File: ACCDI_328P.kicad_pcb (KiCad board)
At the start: 2 copper layers, 150.1 x 82.2 mm, 44 parts, among them IC1 MJE340G, J1 Conn_01x05_Female, Q1 2N2222, Q2 2N2222, U1 LR8N3-G, U2 ATmega328P-P, Y1 16Mhz

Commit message: 2 layer board
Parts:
- added H7: Kill Switch, MountingHole:MountingHole_2.2mm_M2_Pad_TopBottom, F.Cu at (138.3, 115.9)
- R3: footprint Resistor_THT:R_Axial_DIN0516_L15.5mm_D5.0mm_P30.48mm_Horizontal -> Resistor_THT:R_Axial_DIN0516_L15.5mm_D5.0mm_P20.32mm_Horizontal
- Y1: value 16Mhz -> HC49S-16-30-50-70-30-ATF; footprint ABLS2-12:XTAL_ABLS2-12.000MHZ-B1U-T -> Crystal:Resonator-2Pin_W10.0mm_H5.0mm
- moved D2 93.9 mm to (114.9, 57.1)
- moved H4 87.5 mm to (163.4, 115.8)
- moved H3 76.3 mm to (170.9, 115.7)
- moved D3 58.7 mm to (173.4, 108.5)
- moved D5 58.2 mm to (90.8, 115.2), turned to 0 degrees
- moved R9 56.8 mm to (120.5, 115.1)
- moved C7 51.5 mm to (132.8, 69.2)
- moved D1 44.5 mm to (130.6, 62.9), turned to 0 degrees
- moved H5 43.3 mm to (132.1, 116.0)
- moved R6 42.5 mm to (159.8, 109.5)
- moved D8 41.0 mm to (134.4, 102.4)
- moved R4 38.2 mm to (152.7, 56.0), turned to 0 degrees
- moved R5 30.7 mm to (170.9, 56.0)
- moved C4 30.0 mm to (142.2, 71.3), turned to 0 degrees
- moved D7 27.6 mm to (154.9, 70.6)
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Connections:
- IC1 pad 3: Souce_coil -> Net-(IC1-Pad3)
- R4 pad 1: Souce_coil -> Net-(IC1-Pad3)
- U1 pad 2: Souce_coil -> Net-(IC1-Pad3)
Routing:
- net GND: track 425.9 -> 292.3 mm, vias 2 -> 0
- net Souce_coil: track 235.8 -> 132.4 mm
- net SCR_gate: track 128.8 -> 68.7 mm
- net +5 Volt: track 215.8 -> 176.5 mm, vias 5 -> 3
- net Net-(C12-Pad1): track 23.1 -> 59.9 mm
- net Net-(J1-Pad3): track 36.9 -> 73.7 mm
- net Pickup_circuit: track 40.9 -> 66.3 mm, vias 2 -> 0
- net Net-(D8-Pad1): track 18.8 -> 40.8 mm
- net Net-(C10-Pad1): track 48.4 -> 68.0 mm
- net Net-(C9-Pad1): track 20.0 -> 38.3 mm
- net Net-(IC1-Pad3): track 0.00 -> 15.7 mm
- net Net-(C8-Pad2): track 21.9 -> 32.0 mm
- net Net-(R4-Pad2): track 25.3 -> 16.5 mm
- net Net-(C5-Pad1): track 61.1 -> 55.5 mm
- net Net-(C1-Pad2): track 9.32 -> 5.17 mm
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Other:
- board size 150.1 x 82.2 mm -> 100 x 69.1 mm

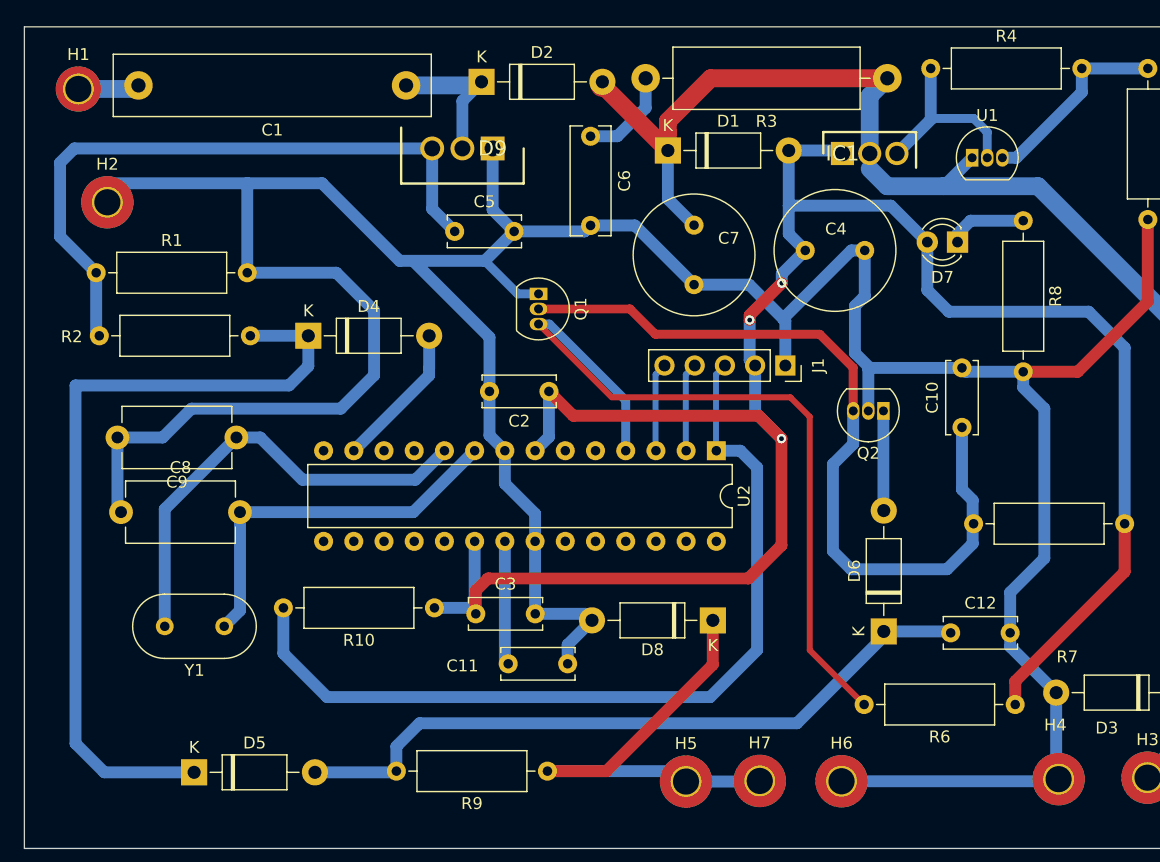
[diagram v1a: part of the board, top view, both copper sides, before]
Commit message: Modified track widths
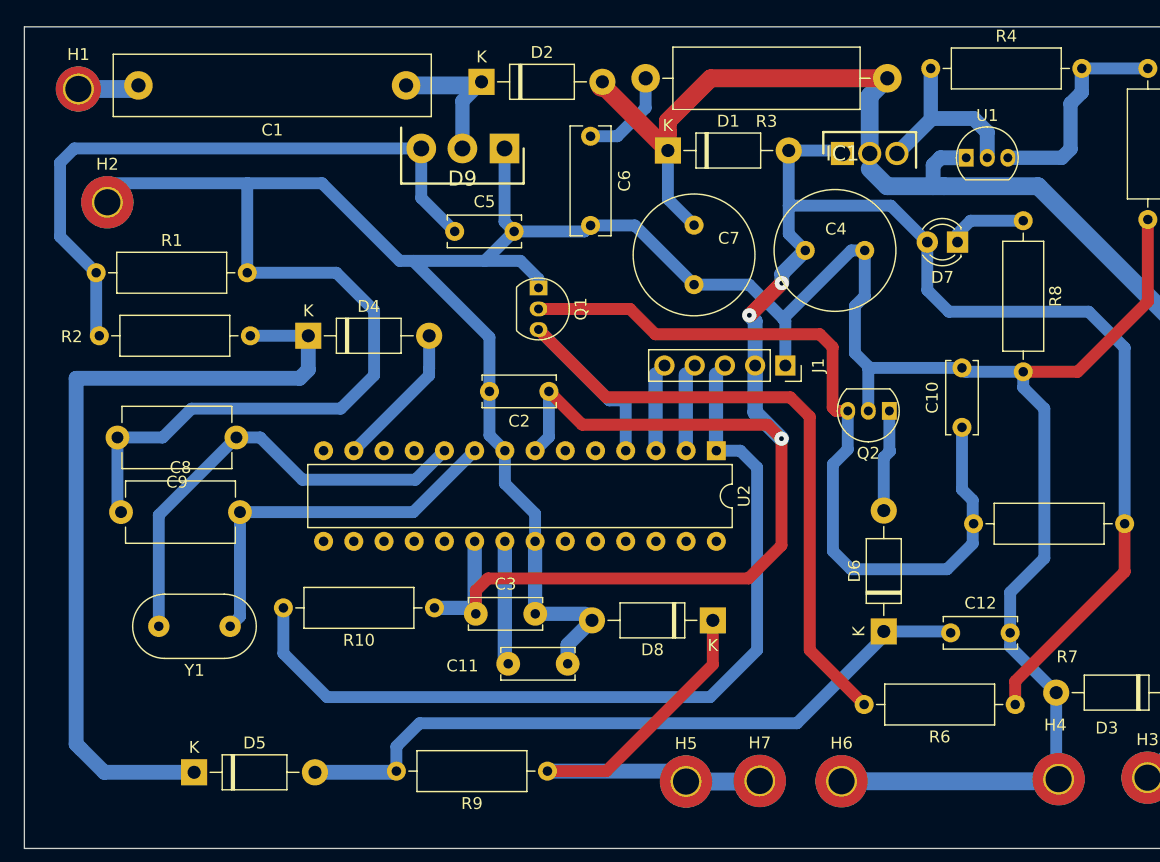
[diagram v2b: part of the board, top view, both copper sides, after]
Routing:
- net Net-(R4-Pad2): track 16.5 -> 18.3 mm
- net Souce_coil: track 132.4 -> 133.8 mm
- net SCR_gate: track 68.7 -> 69.8 mm
- net Net-(C5-Pad1): track 55.5 -> 54.9 mm

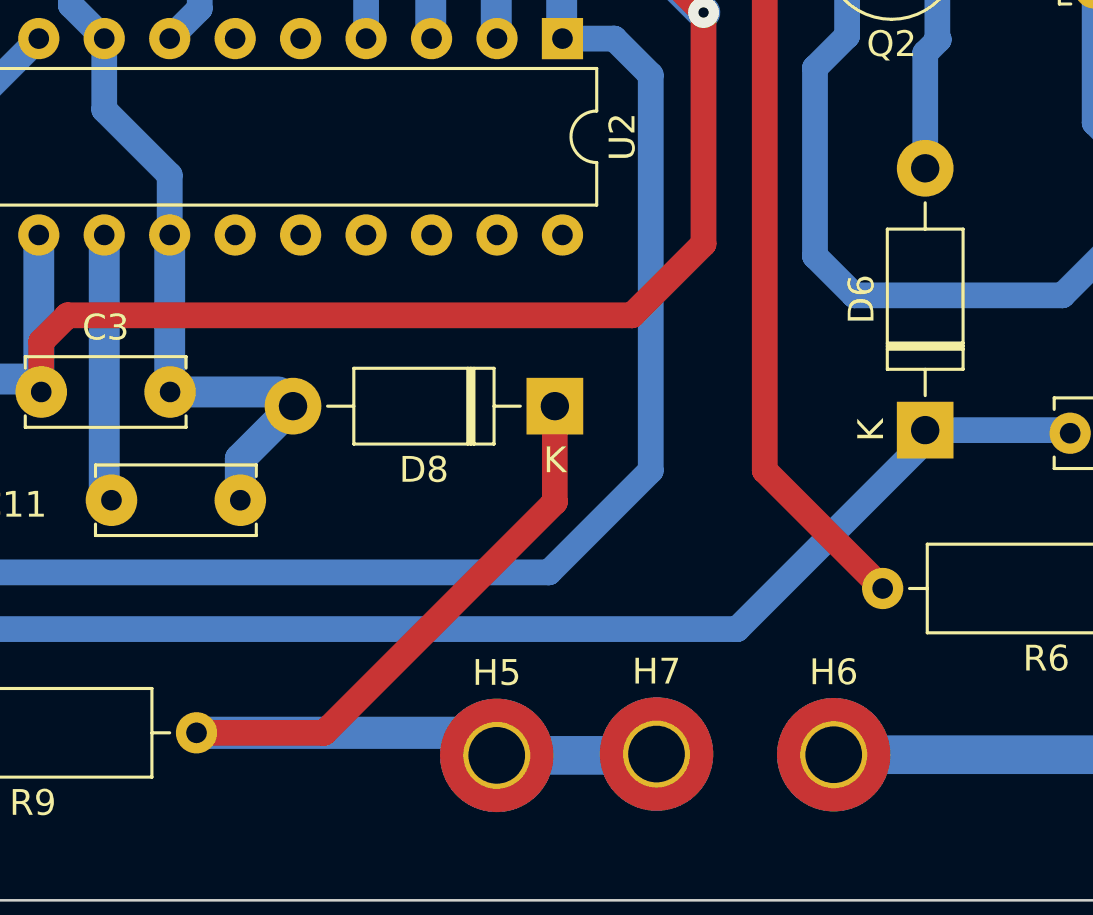
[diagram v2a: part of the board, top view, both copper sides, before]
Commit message: Removed zenner diode
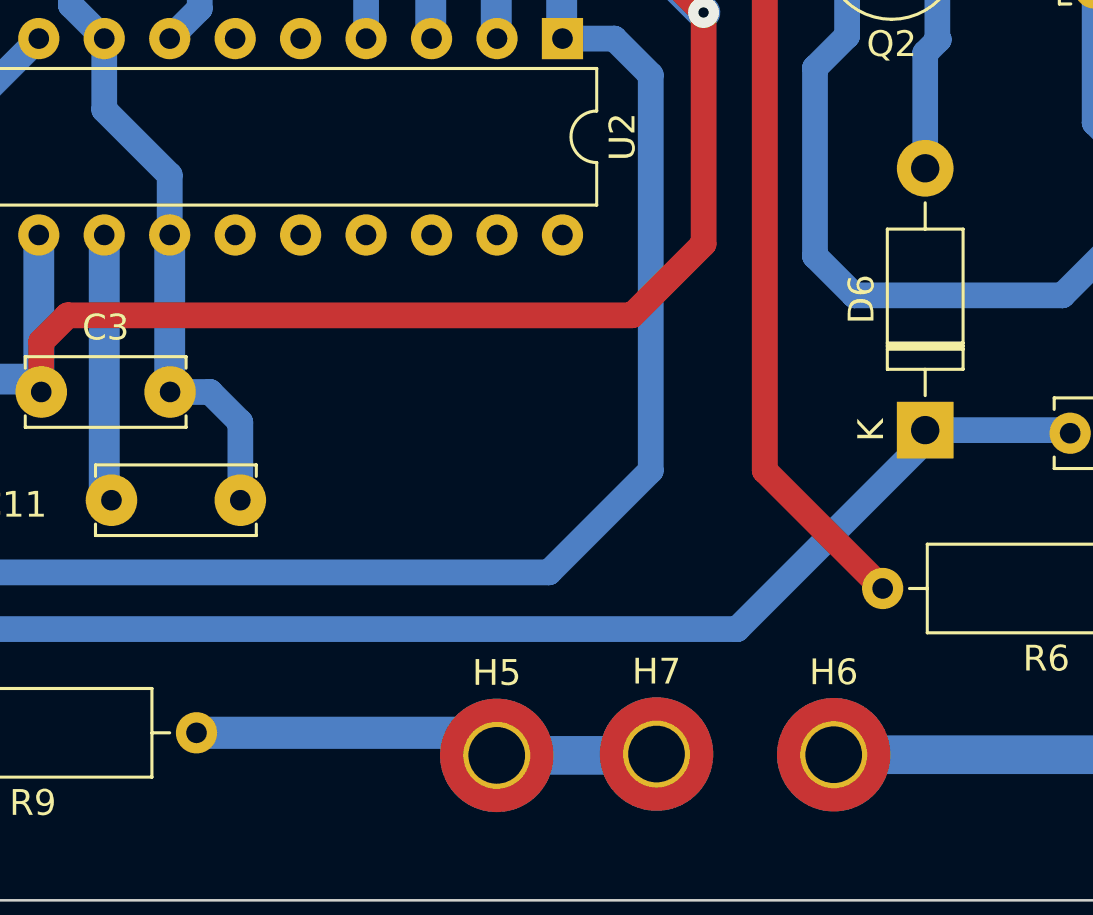
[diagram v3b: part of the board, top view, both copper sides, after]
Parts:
- removed D8: 1N4732 4.7v, Diode_THT:D_DO-41_SOD81_P10.16mm_Horizontal
- R2: value R -> 120
- R9: value 680 -> 560 2 watt
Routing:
- net Net-(H5-Pad1): track 40.8 -> 19.3 mm
- net GND: track 292.1 -> 288.9 mm

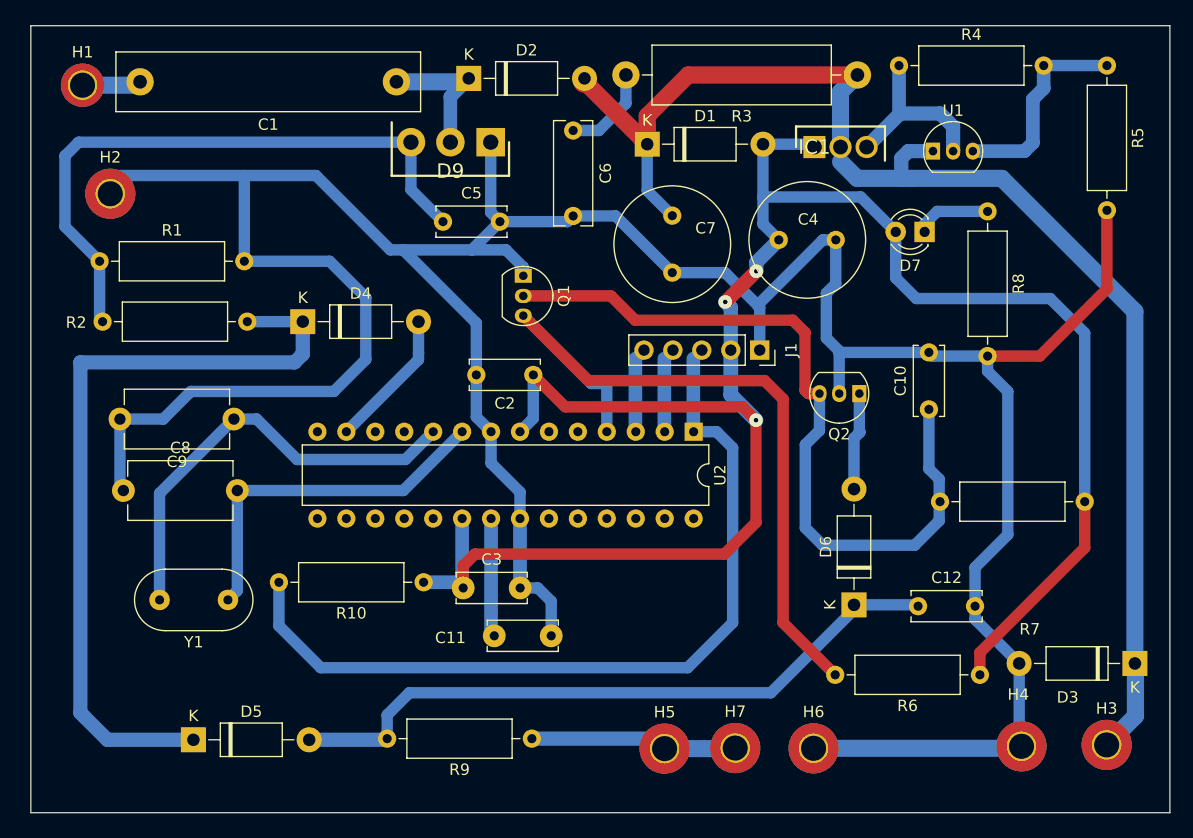
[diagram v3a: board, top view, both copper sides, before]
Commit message: Diodes and reroute
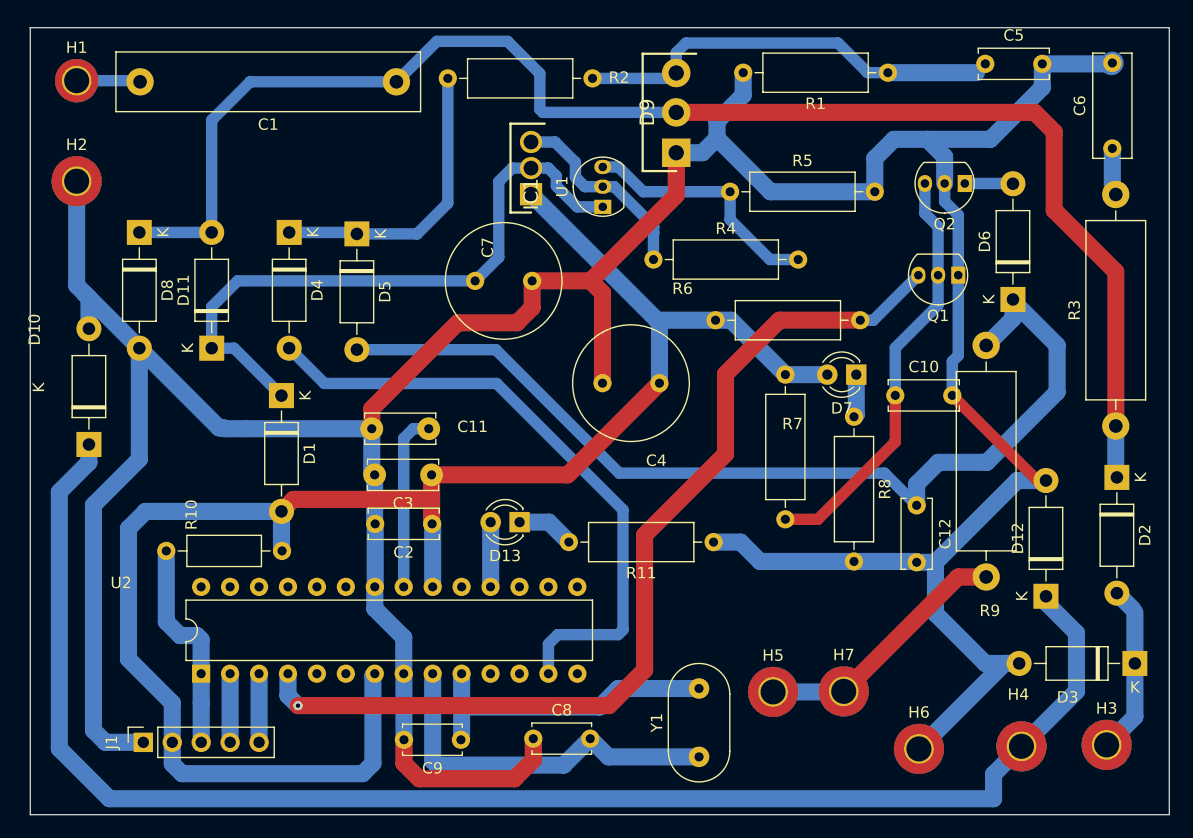
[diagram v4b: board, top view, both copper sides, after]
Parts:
- added D10: D, Diode_THT:D_DO-41_SOD81_P10.16mm_Horizontal, F.Cu at (81.6, 89.3)
- added D11: D, Diode_THT:D_DO-41_SOD81_P10.16mm_Horizontal, F.Cu at (92.4, 80.8)
- added D12: D, Diode_THT:D_DO-41_SOD81_P10.16mm_Horizontal, F.Cu at (165.6, 102.6)
- added D13: LED, LED_THT:LED_D3.0mm, F.Cu at (119.4, 96.1)
- added D8: D, Diode_THT:D_DO-41_SOD81_P10.16mm_Horizontal, F.Cu at (86.0, 70.7)
- added R11: 330, Resistor_THT:R_Axial_DIN0309_L9.0mm_D3.2mm_P12.70mm_Horizontal, F.Cu at (136.4, 97.8)
- C8, C9: footprint Capacitor_THT:C_Disc_D9.0mm_W5.0mm_P10.00mm -> Capacitor_THT:C_Disc_D5.0mm_W2.5mm_P5.00mm
- R10: footprint Resistor_THT:R_Axial_DIN0309_L9.0mm_D3.2mm_P12.70mm_Horizontal -> Resistor_THT:R_Axial_DIN0207_L6.3mm_D2.5mm_P10.16mm_Horizontal
- R9: footprint Resistor_THT:R_Axial_DIN0309_L9.0mm_D3.2mm_P12.70mm_Horizontal -> Resistor_THT:R_Axial_DIN0516_L15.5mm_D5.0mm_P20.32mm_Horizontal
- moved R1 71.1 mm to (151.7, 56.6), turned to 180 degrees
- moved D2 66.8 mm to (171.8, 92.2), turned to -90 degrees
- moved J1 64.1 mm to (86.4, 115.4), turned to 90 degrees
- moved C5 49.6 mm to (160.3, 55.9)
- moved U2 48.2 mm to (91.5, 109.4), turned to 90 degrees
- moved R2 48.0 mm to (125.8, 57.1), turned to 180 degrees
- moved C6 47.4 mm to (171.4, 63.3), turned to 90 degrees
- moved D5 46.7 mm to (105.1, 70.8), turned to -90 degrees
- moved Y1 43.9 mm to (135.2, 116.2), turned to 90 degrees
- moved R9 42.3 mm to (160.3, 100.9), turned to 90 degrees
- moved C8 42.1 mm to (120.6, 115.1)
- moved D1 39.0 mm to (98.5, 85.0), turned to -90 degrees
- moved R6 38.8 mm to (136.6, 78.4), turned to 0 degrees
- moved R3 38.3 mm to (171.7, 87.7), turned to 90 degrees
- moved Q1 37.7 mm to (157.4, 74.4), turned to 180 degrees
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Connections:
- C1 pad 1: Souce_coil -> From_source_coil
- C7 pad 1: Souce_coil -> Net-(C7-Pad1)
- D1 pad 1: Souce_coil -> Net-(C7-Pad1)
- D2 pad 1: Souce_coil -> From_source_coil
- D9 pad 2: Souce_coil -> From_source_coil
- H4 pad 1: GND -> Source coil -
- IC1 pad 2: Souce_coil -> Net-(C7-Pad1)
- R3 pad 1: Souce_coil -> From_source_coil
- U1 pad 1: Souce_coil -> Net-(C7-Pad1)
- U2 pad 18: unconnected-(U2-Pad18) -> Net-(U2-Pad18)
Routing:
- net Source coil -: track 0.00 -> 133.5 mm
- net From_source_coil: track 0.00 -> 130.7 mm
- net Souce_coil: track 133.8 -> 15.0 mm
- net Net-(C7-Pad1): track 0.00 -> 56.7 mm
- net Net-(J1-Pad3): track 73.7 -> 18.9 mm
- net SCR_gate: track 69.8 -> 26.0 mm
- net Net-(D4-Pad2): track 12.3 -> 55.4 mm
- net GND: track 288.9 -> 327.9 mm
- net Net-(C10-Pad1): track 68.2 -> 37.2 mm
- net Net-(C12-Pad1): track 59.9 -> 87.1 mm
- net +5 Volt: track 176.5 -> 151.1 mm, vias 3 -> 0
- net Pickup_circuit: track 66.0 -> 84.3 mm, vias 0 -> 1
- net Net-(C5-Pad1): track 54.9 -> 38.2 mm
- net Net-(C9-Pad1): track 38.5 -> 27.5 mm
- net Net-(U2-Pad18): track 0.00 -> 5.68 mm
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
